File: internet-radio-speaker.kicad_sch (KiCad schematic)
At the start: 22 parts, among them J1 USB_C_Receptacle_USB2.0, Q1 DMP1045U, U3 USBLC6-2SC6, U4 M3406

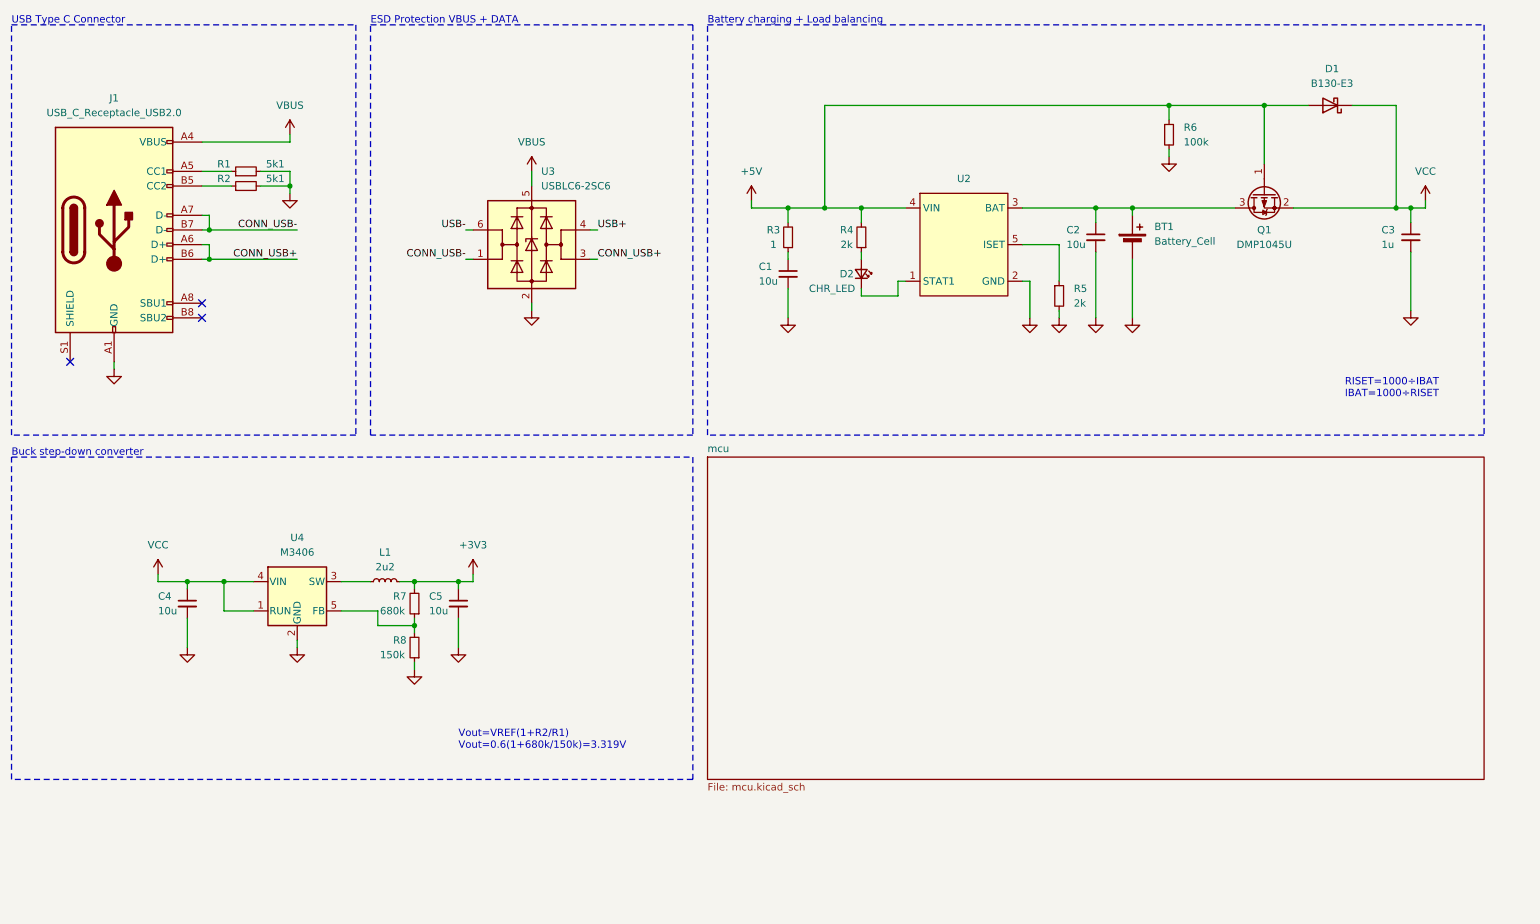
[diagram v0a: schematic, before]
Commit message: Added potentiometer and fixed amplifiers
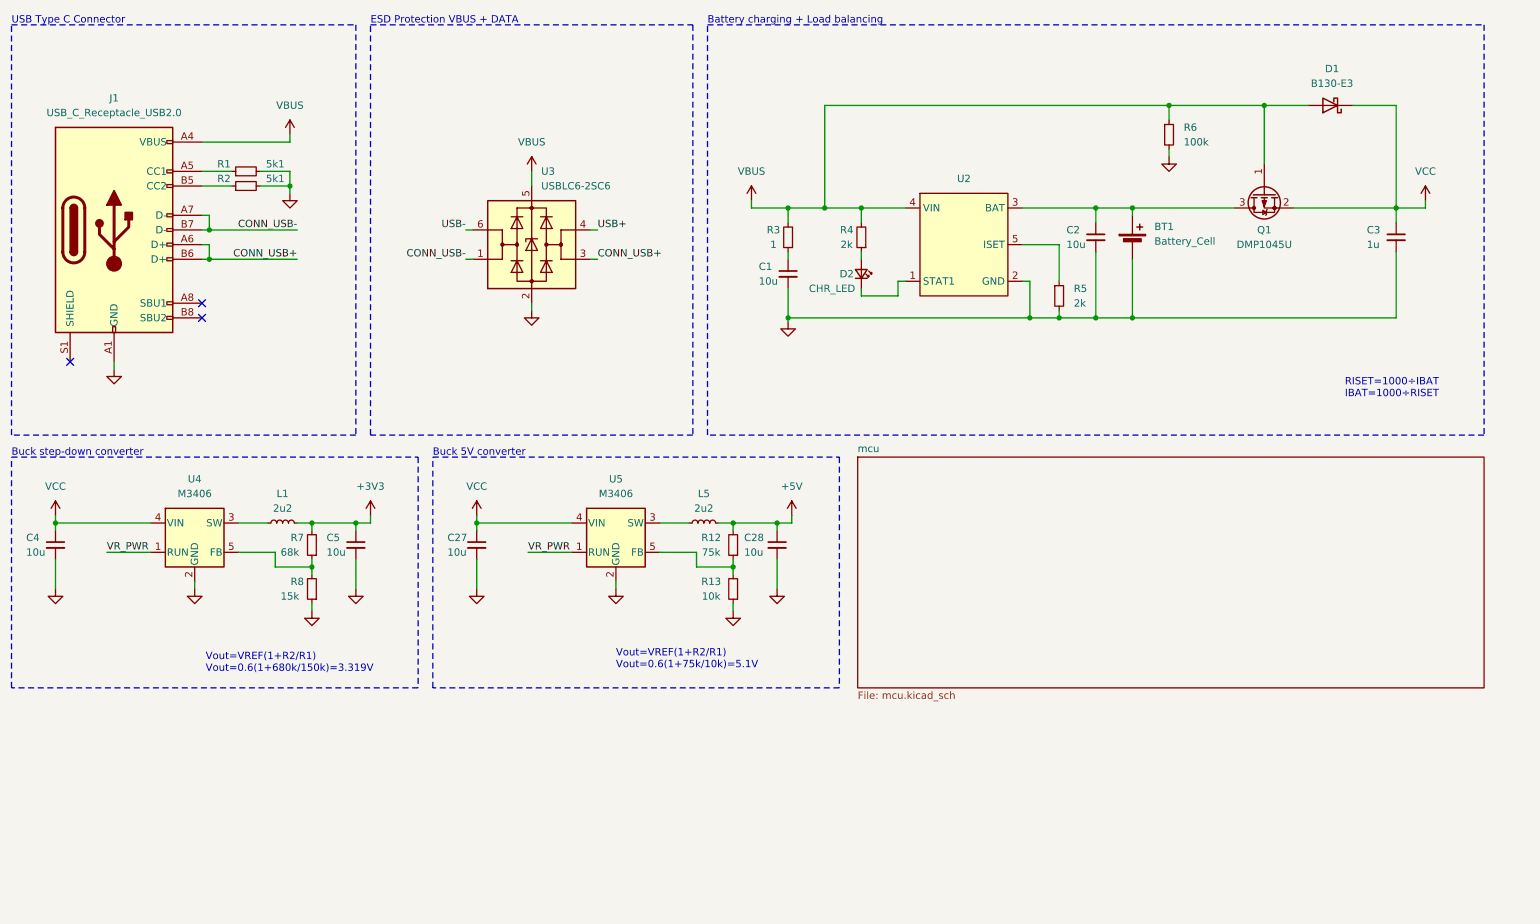
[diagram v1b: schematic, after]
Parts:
- added C27, C28: 10u, symbol Device:C_Small
- added L5: 2u2, symbol Device:L_Small
- added R12: 75k, symbol Device:R_Small
- added R13: 10k, symbol Device:R_Small
- added U5: M3406, Package_TO_SOT_SMD:SOT-23-5, symbol custom_library:M3406
- R7: value 680k -> 68k
- R8: value 150k -> 15k
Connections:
- net +5V: now also C28.1, L5.2, R12.2; no longer D1.2 (A), Q1.1 (G), R3.2, R4.2, R6.1, U2.4 (VIN)
- net GND: now also C27.2, C28.2, R13.1, U5.2 (GND)
- net VBUS: now also D1.2 (A), Q1.1 (G), R3.2, R4.2, R6.1, U2.4 (VIN)
- net VCC: now also C27.1, U5.4 (VIN); no longer U4.1 (RUN)
- new net: L5.1, U5.3 (SW)
- new net: R12.1, R13.2, U5.5 (FB)
- new net VR_PWR: U4.1 (RUN), U5.1 (RUN)
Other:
- note added: "Buck 5V converter"
- note added: "Vout=VREF(1+R2/R1) Vout=0.6(1+75k/10k)=5.1V"
- moved on the sheet: C3, C4, C5, L1, R7, R8, U4

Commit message: Finished rev 1 of the board
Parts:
- removed BT1: Battery_Cell, symbol Device:Battery_Cell
- removed C4: 10u, symbol Device:C_Small
- removed Q1: DMP1045U, Package_TO_SOT_SMD:SOT-23, symbol custom_library:DMP1045U
- removed R12: 75k, symbol Device:R_Small
- removed R13: 10k, symbol Device:R_Small
- removed R3: 1, symbol Device:R_Small
- removed U2: ~, Package_TO_SOT_SMD:SOT-23-5, symbol custom_library:LP4054H
- removed U4, U5: M3406, Package_TO_SOT_SMD:SOT-23-5, symbol custom_library:M3406
- added C2, C6: 100n, Capacitor_SMD:C_0402_1005Metric, symbol Device:C_Small
- added C7, C8: 10u, Capacitor_SMD:C_0603_1608Metric, symbol Device:C_Small
- added J2: BAT_CON, Connector_Wire:SolderWire-0.5sqmm_1x02_P4.6mm_D0.9mm_OD2.1mm, symbol Connector:Conn_01x02_Pin
- added Q1: DMP1045U-7, Internet_Radio_Speaker:SOT96P240X120-3N, symbol DMP1045U-7:DMP1045U-7
- added R10, R6: 100, Resistor_SMD:R_0402_1005Metric, symbol Device:R_Small
- added R9: 200k, Resistor_SMD:R_0402_1005Metric, symbol Device:R_Small
- added U101: LP4054H, Package_TO_SOT_SMD:SOT-23-5, symbol LP4054H:LP4054H
- added U4: XC9141, Internet_Radio_Speaker:SOT95P280X130-5N, symbol XC9141:XC9141
- added U8: TPS63000, Package_SON:Texas_DRC0010J_ThermalVias, symbol Regulator_Switching:TPS63000
- added VR1: ~, Internet_Radio_Speaker:Potentiometer_Alps_RK0971111Z1P, symbol P0915S:P0915S
- C1, C5: footprint (none) -> Capacitor_SMD:C_0603_1608Metric; LCSC (none) -> C15525
- C10: renamed from C28; footprint (none) -> Capacitor_SMD:C_0603_1608Metric; LCSC (none) -> C15525
- C3: renamed from C2; footprint (none) -> Capacitor_SMD:C_0603_1608Metric; LCSC (none) -> C15525
- C4: renamed from C3; value 1u -> 10u; footprint (none) -> Capacitor_SMD:C_0603_1608Metric; LCSC (none) -> C15525
- C9: renamed from C27; footprint (none) -> Capacitor_SMD:C_0603_1608Metric; LCSC (none) -> C15525
- D1: renamed from D2; footprint (none) -> LED_SMD:LED_0603_1608Metric; LCSC (none) -> C2286
- D2: renamed from D1; value B130-E3 -> SS14; LCSC (none) -> C2480
- J1: value USB_C_Receptacle_USB2.0 -> USB-TYPE-C-018; footprint (none) -> Connector_USB:USB_C_Receptacle_GCT_USB4105-xx-A_16P_TopMnt_Horizontal; LCSC (none) -> C2927038
- L1: footprint (none) -> Inductor_SMD:L_0805_2012Metric; LCSC (none) -> C2049745
- L2: renamed from L5; value 2u2 -> 4u7; footprint (none) -> Inductor_SMD:L_1008_2520Metric; LCSC (none) -> C668313
- R1, R2: footprint (none) -> Resistor_SMD:R_0402_1005Metric; LCSC (none) -> C25905
- R3: renamed from R4; footprint (none) -> Resistor_SMD:R_0402_1005Metric; LCSC (none) -> C4109
- R4: renamed from R5; footprint (none) -> Resistor_SMD:R_0402_1005Metric; LCSC (none) -> C4109
- R5: renamed from R6; footprint (none) -> Resistor_SMD:R_0402_1005Metric; LCSC (none) -> C25741
- R7: value 68k -> 100; footprint (none) -> Resistor_SMD:R_0402_1005Metric; LCSC (none) -> C25076
- R8: value 15k -> 1M; footprint (none) -> Resistor_SMD:R_0402_1005Metric; LCSC (none) -> C26083
- U1: renamed from U3; LCSC (none) -> C435848
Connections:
- net +3V3: now also R8.2, C7.1, C8.1, U8.1 (VOUT); no longer C5.1, L1.2, R7.2
- net +5V: now also U4.4 (VOUT); no longer L2.2
- net GND: now also C2.2, C6.2, C7.2, C8.2, J2.2 (Pin_2), R9.1, U101.2 (GND), U4.2 (GND), U8.11 (PGND), U8.3 (PGND), U8.9 (GND); no longer R8.1
- net VBUS: now also C1.1, Q1.1 (G), U101.4 (VIN)
- net VCC: now also C5.1, L2.1, Q1.2 (S), R6.2, U4.3 (BAT), U8.5 (VIN), VR1.4 (A)
- net VR_PWR: now also R7.1, VR1.5 (B)
- net CC1: now reaches J1.A5 (CC1), R1.1
- net CC2: now reaches J1.B5 (CC2), R2.1
- net BAT_CON_P: now reaches C3.1
- net BAT_CON_P: now also J2.1 (Pin_1), Q1.3 (D), U101.3 (BAT)
- net ISET: now reaches R4.1
- net ISET: now also U101.5 (ISET)
- net L2: now reaches L1.1
- net L2: now also U8.2 (L2)
- net LED: now reaches D1.2 (A), R3.1
- net mcu/BAT_STAT: now reaches D1.1 (K)
- net mcu/BAT_STAT: now also C2.1, U101.1 (STAT1)
- net CONN_USB+ renamed CONN_USB_D+
- net CONN_USB- renamed CONN_USB_D-
- net USB+ renamed USB_D+
- net USB- renamed USB_D-
- new net AMP_SW: R10.1
- new net CE: R10.2, U4.1 (CE)
- new net EN: R7.2, U8.6 (EN)
- new net FB: R8.1, R9.2, U8.10 (FB)
- new net L1: L1.2, U8.4 (L1)
- new net LX: L2.2, U4.5 (LX)
- new net VINA: C6.1, R6.1, U8.7 (PS/SYNC), U8.8 (VINA)
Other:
- added sheet Amplifiers (amp.kicad_sch)
- sheet mcu ports: added AMP_SW, BAT_STAT; removed none
- note added: "500mA charging current"
- note added: "Boost 5V converter"
- note added: "Buck-Boost converter"
- note added: "L1 1.2A"
- note added: "L2 1.5A"
- note added: "Potentiometer w/ switch"
- note added: "R8 & R9 Feedback resistors"
- note removed: "Buck 5V converter"
- note removed: "Buck step-down converter"
- note removed: "Vout=VREF(1+R2/R1) Vout=0.6(1+680k/150k)=3.319V"
- note removed: "Vout=VREF(1+R2/R1) Vout=0.6(1+75k/10k)=5.1V"
- company: SInisha Stojchevski -> ST
- moved on the sheet: C1, C10, C3, C9, D1, L2, R1, R2, R3

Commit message: updated to rev 3
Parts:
- removed C1, C10, C3, C4, C5, C7, C8, C9: 10u, Capacitor_SMD:C_0603_1608Metric, symbol Device:C_Small
- removed C2, C6: 100n, Capacitor_SMD:C_0402_1005Metric, symbol Device:C_Small
- removed D1: CHR_LED, LED_SMD:LED_0603_1608Metric, symbol Device:LED_Small
- removed D2: SS14, Diode_SMD:D_SMA, symbol Diode:B130-E3
- removed J2: BAT_CON, Connector_Wire:SolderWire-0.5sqmm_1x02_P4.6mm_D0.9mm_OD2.1mm, symbol Connector:Conn_01x02_Pin
- removed L1: 2u2, Inductor_SMD:L_0805_2012Metric, symbol Device:L_Small
- removed L2: 4u7, Inductor_SMD:L_1008_2520Metric, symbol Device:L_Small
- removed Q1: DMP1045U-7, Internet_Radio_Speaker:SOT96P240X120-3N, symbol DMP1045U-7:DMP1045U-7
- removed R10, R6, R7: 100, Resistor_SMD:R_0402_1005Metric, symbol Device:R_Small
- removed R3, R4: 2k, Resistor_SMD:R_0402_1005Metric, symbol Device:R_Small
- removed R5: 100k, Resistor_SMD:R_0402_1005Metric, symbol Device:R_Small
- removed R8: 1M, Resistor_SMD:R_0402_1005Metric, symbol Device:R_Small
- removed R9: 200k, Resistor_SMD:R_0402_1005Metric, symbol Device:R_Small
- removed U101: LP4054H, Package_TO_SOT_SMD:SOT-23-5, symbol LP4054H:LP4054H
- removed U4: XC9141, Internet_Radio_Speaker:SOT95P280X130-5N, symbol XC9141:XC9141
- removed U8: TPS63000, Package_SON:Texas_DRC0010J_ThermalVias, symbol Regulator_Switching:TPS63000
- added C101, C105, C107: 10u, Capacitor_SMD:C_0805_2012Metric, symbol Device:C_Polarized_Small
- added C102: DNP, Capacitor_SMD:C_0805_2012Metric, symbol Device:C_Polarized_Small
- added C103: 10n, Capacitor_SMD:C_0603_1608Metric, symbol Device:C_Small
- added C104: 100n, Capacitor_SMD:C_0603_1608Metric, symbol Device:C_Small
- added D101: PWR_LED, LED_SMD:LED_0805_2012Metric, symbol Device:LED
- added H101, H102, H103, H104: MountingHole_Pad, MountingHole:MountingHole_2.7mm_M2.5_DIN965_Pad, symbol Mechanical:MountingHole_Pad
- added J203: EXT_PWR, Connector_PinHeader_2.54mm:PinHeader_1x02_P2.54mm_Vertical, symbol Connector:Conn_01x02_Pin
- added L203: 3u3, Inductor_SMD:L_0805_2012Metric, symbol Device:L_Small
- added R101: 10k, Resistor_SMD:R_0603_1608Metric, symbol Device:R_Small
- added R102: 5k1, Resistor_SMD:R_0603_1608Metric, symbol Device:R_Small
- added U101: TC1263, Package_SO:SOIC-8_3.9x4.9mm_P1.27mm, symbol TC1263:TC1263
- J1: value USB-TYPE-C-018 -> USB_C_Receptacle_USB2.0; LCSC C2927038 -> (none)
- R1, R2: footprint Resistor_SMD:R_0402_1005Metric -> Resistor_SMD:R_0603_1608Metric; LCSC C25905 -> (none)
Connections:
- net VCC is gone; now on net +5V: VR1.4 (A)
- net +3V3: now also C101.1, D101.2 (A), J203.1 (Pin_1), U101.1 (VOUT)
- net +5V: now also U1.5 (VBUS), C104.1, C105.1, C107.1, L203.2, U101.8 (VIN)
- net GND: now also C101.2, C102.2, C103.2, C104.2, C105.2, C107.2, H101.1, H102.1, H103.1, H104.1, J203.2 (Pin_2), R102.2, U101.2 (GND)
- net VBUS: now also C103.1, L203.1; no longer U1.5 (VBUS)
- net VR_PWR: now also R101.2
- net CC1: no longer names the net of J1.A5 (CC1), R1.1
- net CC2: no longer names the net of J1.B5 (CC2), R2.1
- new net: C102.1, U101.4 (BYPASS)
- new net: R101.1, U101.6 (SHDN)
- new net: D101.1 (K), R102.1
- no-connect marks 3 -> 4
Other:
- sheet mcu renamed Microcontroller
- sheet Amplifiers ports: added AMP_SW, I2S0_BCK_IN, I2S0_SD_IN, I2S0_WS_IN; removed none
- sheet Microcontroller ports: added I2S0_BCK_OUT, I2S0_SD_OUT, I2S0_WS_OUT; removed none
- note added: "ESD Protection"
- note added: "LDO Converter (VBUS 4V5-5V5 to 3V3)"
- note added: "USB Type C Connector / VBUS Filter"
- note removed: "500mA charging current"
- note removed: "Battery charging + Load balancing"
- note removed: "Boost 5V converter"
- note removed: "Buck-Boost converter"
- note removed: "ESD Protection VBUS + DATA"
- note removed: "L1 1.2A"
- note removed: "L2 1.5A"
- note removed: "R8 & R9 Feedback resistors"
- note removed: "RISET=1000÷IBAT IBAT=1000÷RISET"
- note removed: "USB Type C Connector"
- moved on the sheet: U1, VR1A

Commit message: updated to rev 4
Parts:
- removed C102: DNP, Capacitor_SMD:C_0805_2012Metric, symbol Device:C_Polarized_Small
- removed H101: MountingHole_Pad, MountingHole:MountingHole_2.7mm_M2.5_DIN965_Pad, symbol Mechanical:MountingHole_Pad
- removed J203: EXT_PWR, Connector_PinHeader_2.54mm:PinHeader_1x02_P2.54mm_Vertical, symbol Connector:Conn_01x02_Pin
- removed L203: 3u3, Inductor_SMD:L_0805_2012Metric, symbol Device:L_Small
- removed U101: TC1263, Package_SO:SOIC-8_3.9x4.9mm_P1.27mm, symbol TC1263:TC1263
- added FB101: BLM21SP601SN1D, Inductor_SMD:L_0805_2012Metric, symbol Device:FerriteBead_Small
- added R103: 1k, Resistor_SMD:R_0402_1005Metric, symbol Device:R_Small
- added TP101: 5V_TP, TestPoint:TestPoint_Pad_D1.5mm, symbol Connector:TestPoint_Small
- added TP102: 3V3_TP, TestPoint:TestPoint_Pad_D1.5mm, symbol Connector:TestPoint_Small
- added U102: AP2112K-3.3, Package_TO_SOT_SMD:SOT-23-5, symbol Regulator_Linear:AP2112K-3.3
- C101, C105, C107: footprint Capacitor_SMD:C_0805_2012Metric -> Capacitor_SMD:C_0603_1608Metric; JLCPCB Part # (none) -> C96446
- C103: footprint Capacitor_SMD:C_0603_1608Metric -> Capacitor_SMD:C_0402_1005Metric; JLCPCB Part # (none) -> C15195
- C104: footprint Capacitor_SMD:C_0603_1608Metric -> Capacitor_SMD:C_0402_1005Metric; JLCPCB Part # (none) -> C1525
- D101: footprint LED_SMD:LED_0805_2012Metric -> LED_SMD:LED_0603_1608Metric; JLCPCB Part # (none) -> C2286; LCSC C72041 -> (none)
- H102, H103, H104: footprint MountingHole:MountingHole_2.7mm_M2.5_DIN965_Pad -> MountingHole:MountingHole_2.7mm_M2.5_Pad_Via
- J1: JLCPCB Part # (none) -> C2927038
- R1, R2: footprint Resistor_SMD:R_0603_1608Metric -> Resistor_SMD:R_0402_1005Metric; JLCPCB Part # (none) -> C25905
- R101: value 10k -> 5k1; footprint Resistor_SMD:R_0603_1608Metric -> Resistor_SMD:R_0402_1005Metric; JLCPCB Part # (none) -> C25905
- R102: value 5k1 -> 1k; footprint Resistor_SMD:R_0603_1608Metric -> Resistor_SMD:R_0402_1005Metric; JLCPCB Part # (none) -> C11702; LCSC C25905 -> (none)
- U1: JLCPCB Part # (none) -> C2687116; LCSC C435848 -> (none)
- VR1: JLCPCB Part # (none) -> C2687318; LCSC C2687318 -> (none)
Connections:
- net +3V3: now also TP102.1, U102.5 (VOUT)
- net +5V: now also FB101.2, TP101.1, U102.1 (VIN)
- net GND: now also R101.2, U102.2 (GND)
- net VBUS: now also FB101.1
- net VR_PWR: now also R101.1, R103.2; no longer R101.2
- new net EN: R103.1, U102.3 (EN)
- no-connect marks 4 -> 3
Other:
- sheet Microcontroller ports: added none; removed BAT_STAT
- moved on the sheet: C101, C103, C105, C107, D101, H102, H103, H104, R101, R102, U1, VR1A

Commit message: Updated to KiCad 9
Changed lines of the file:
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@@
 (kicad_sch
-	(version 20231120)
+	(version 20250114)
 	(generator "eeschema")
-	(generator_version "8.0")
+	(generator_version "9.0")
 	(paper "A4")
 	(title_block
@@
 		(company "ST")
 	)
+	(rectangle
+		(start 127.635 27.94)
+		(end 183.515 86.995)
+		(stroke
+			(width 0)
+			(type dash)
+		)
+		(fill
+			(type none)
+		)
+	)
+	(rectangle
+		(start 20.32 27.94)
+		(end 125.095 86.995)
+		(stroke
+			(width 0)
+			(type dash)
+		)
+		(fill
+			(type none)
+		)
+	)
+	(rectangle
+		(start 92.202 92.964)
+		(end 150.622 128.778)
+		(stroke
+			(width 0)
+			(type dash)
+		)
+		(fill
+			(type none)
+		)
+	)
+	(rectangle
+		(start 186.055 27.94)
+		(end 283.21 86.995)
+		(stroke
+			(width 0)
+			(type dash)
+		)
+		(fill
+			(type none)
+		)
+	)
+	(text "ESD Protection"
+		(exclude_from_sim no)
+		(at 127 26.67 0)
+		(effects
+			(font
+				(size 1.905 1.905)
+				(thickness 0.381)
+				(bold yes)
+			)
+			(justify left bottom)
+		)
+	)
+	(text "USB Type C Connector / VBUS Filter"
+		(exclude_from_sim no)
+		(at 20.32 26.67 0)
+		(effects
+			(font
+				(size 1.905 1.905)
+				(thickness 0.381)
+				(bold yes)
+			)
+			(justify left bottom)
+		)
+	)
+	(text "Potentiometer w/ switch"
+		(exclude_from_sim no)
+		(at 91.44 91.44 0)
+		(effects
+			(font
+				(size 1.905 1.905)
+				(thickness 0.381)
+				(bold yes)
+			)
+			(justify left bottom)
+		)
+	)
+	(text "LDO Converter (VBUS 4V5-5V5 to 3V3)"
+		(exclude_from_sim no)
+		(at 185.42 26.67 0)
+		(effects
+			(font
+				(size 1.905 1.905)
+				(thickness 0.381)
+				(bold yes)
+			)
+			(justify left bottom)
+		)
+	)
 	(junction
 		(at 68.58 41.91)
@@
 		)
 	)
-	(rectangle
-		(start 127.635 27.94)
-		(end 183.515 86.995)
-		(stroke
-			(width 0)
-			(type dash)
-		)
-		(fill
-			(type none)
-		)
-	)
-	(rectangle
-		(start 20.32 27.94)
-		(end 125.095 86.995)
-		(stroke
-			(width 0)
-			(type dash)
-		)
-		(fill
-			(type none)
-		)
-	)
-	(rectangle
-		(start 92.202 92.964)
-		(end 150.622 128.778)
-		(stroke
-			(width 0)
-			(type dash)
-		)
-		(fill
-			(type none)
-		)
-	)
-	(rectangle
-		(start 186.055 27.94)
-		(end 283.21 86.995)
-		(stroke
-			(width 0)
-			(type dash)
-		)
-		(fill
-			(type none)
-		)
-	)
-	(text "ESD Protection"
-		(exclude_from_sim no)
-		(at 127 26.67 0)
-		(effects
-			(font
-				(size 1.905 1.905)
-				(thickness 0.381)
-				(bold yes)
-			)
-			(justify left bottom)
-		)
-	)
-	(text "USB Type C Connector / VBUS Filter"
-		(exclude_from_sim no)
-		(at 20.32 26.67 0)
-		(effects
-			(font
-				(size 1.905 1.905)
-				(thickness 0.381)
-				(bold yes)
-			)
-			(justify left bottom)
-		)
-	)
-	(text "Potentiometer w/ switch"
-		(exclude_from_sim no)
-		(at 91.44 91.44 0)
-		(effects
-			(font
-				(size 1.905 1.905)
-				(thickness 0.381)
-				(bold yes)
-			)
-			(justify left bottom)
-		)
-	)
-	(text "LDO Converter (VBUS 4V5-5V5 to 3V3)"
-		(exclude_from_sim no)
-		(at 185.42 26.67 0)
-		(effects
-			(font
-				(size 1.905 1.905)
-				(thickness 0.381)
-				(bold yes)
-			)
-			(justify left bottom)
-		)
-	)
 	(label "CONN_USB_D+"
 		(at 116.84 59.69 180)
@@
 		(at 158.75 92.71)
 		(size 50.8 36.322)
+		(exclude_from_sim no)
+		(in_bom yes)
+		(on_board yes)
+		(dnp no)
 		(stroke
 			(width 0.1524)
@@
 		(at 226.06 92.71)
 		(size 57.15 36.576)
+		(exclude_from_sim no)
+		(in_bom yes)
+		(on_board yes)
+		(dnp no)
 		(fields_autoplaced yes)
 		(stroke
@@
 		)
 	)
+	(embedded_fonts no)
 )
